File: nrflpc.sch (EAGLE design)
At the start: 62 parts, among them IC1 LPC1111/12/13/14-HVQFN33, IC3 LM3401, IC5 LM3401, IC6 LM3401, IC7 LM3401, IC8 78L05SMD, Q1 20MHz, Q2 MOSFET-PCHANNEL, Q3 MOSFET-PCHANNEL, Q4 MOSFET-PCHANNEL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

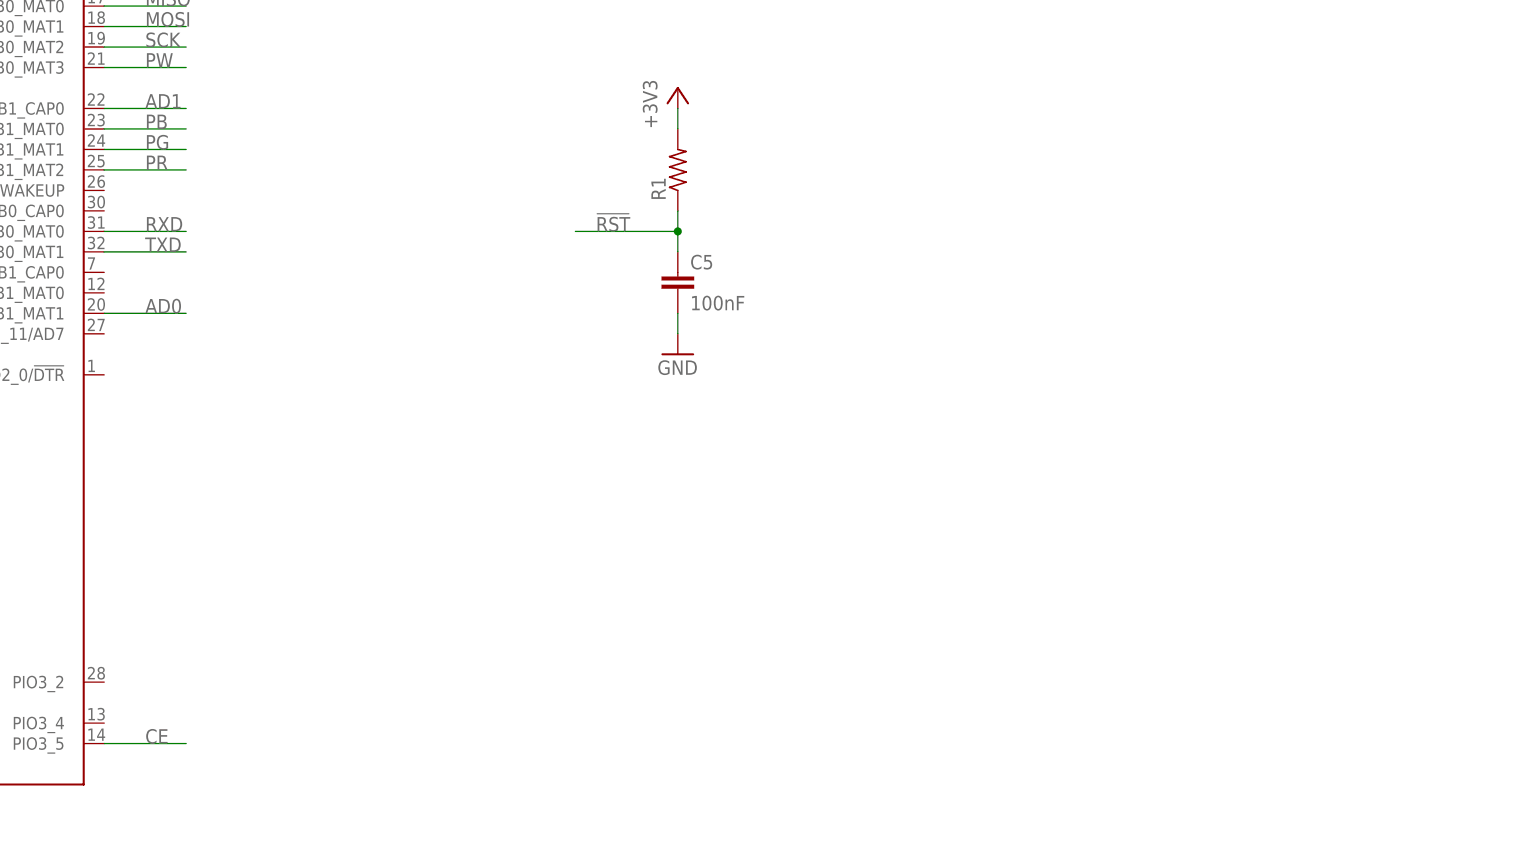
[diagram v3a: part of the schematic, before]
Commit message: ADC input filters
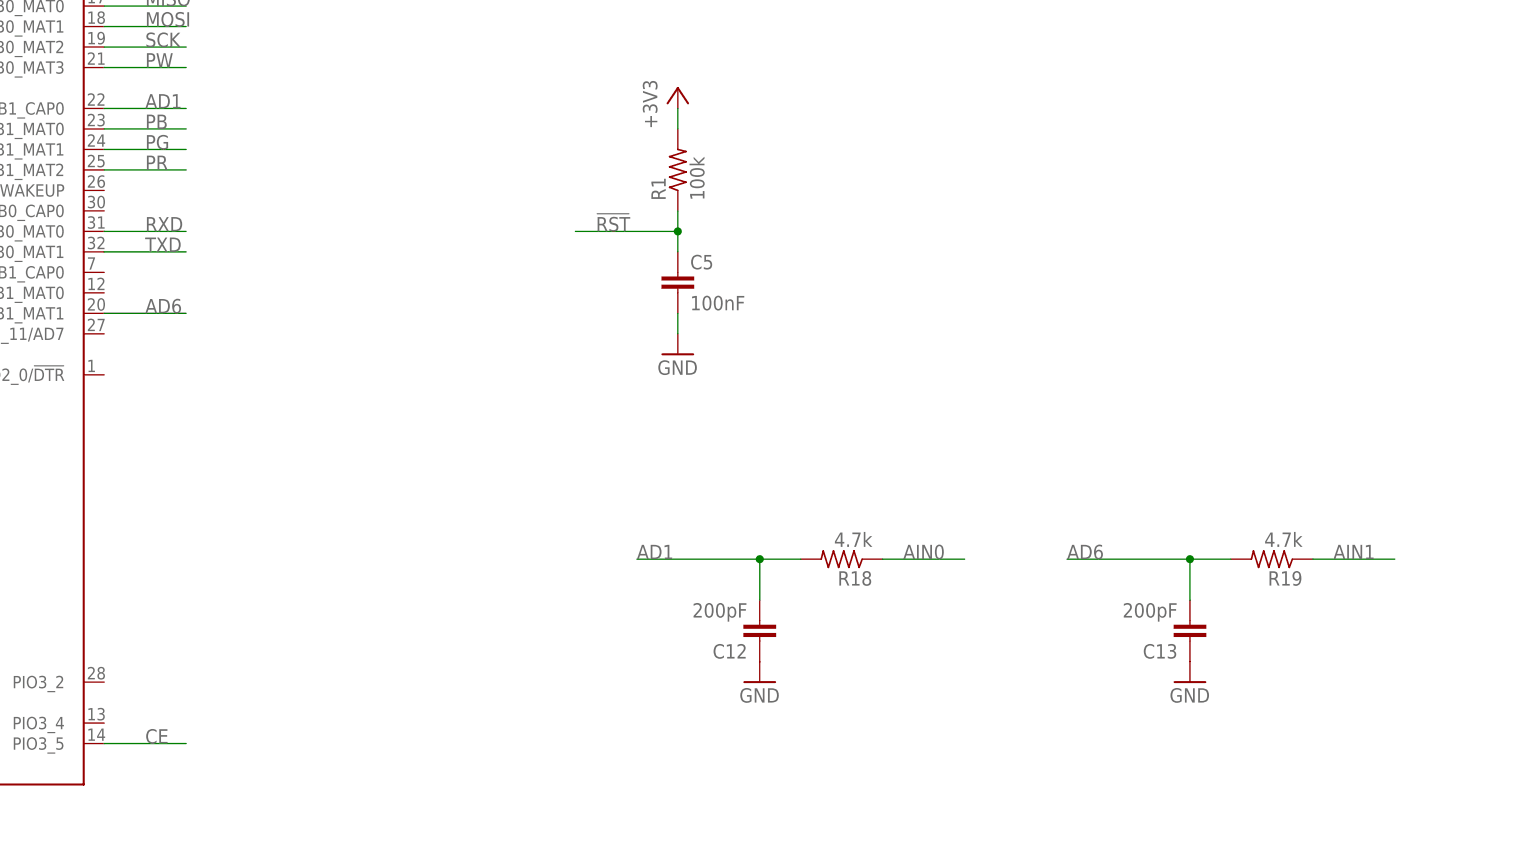
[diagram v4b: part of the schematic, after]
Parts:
- added C12, C13: 200pF, SparkFun:CAP0402-CAP
- added R18, R19: 4.7k, rcl:R-US_R0402
- R1: value (none) -> 100k
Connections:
- removed net AD0: IC1.PIO1_10/AD6/CT16B1_MAT1
- new net AD6: C13.2, IC1.PIO1_10/AD6/CT16B1_MAT1, R19.2
- new net AIN0: R18.1
- new net AIN1: R19.1
- net AD1: now also C12.2, R18.2
- net GND: now also C12.1, C13.1
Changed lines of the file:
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@@
 <part name="C4" library="rcl" deviceset="C-EU" device="C0402" value="100nF"/>
 <part name="GND5" library="supply1" deviceset="GND" device=""/>
-<part name="R1" library="rcl" deviceset="R-US_" device="R0402"/>
+<part name="R1" library="rcl" deviceset="R-US_" device="R0402" value="100k"/>
 <part name="+3V5" library="supply1" deviceset="+3V3" device=""/>
 <part name="GND13" library="supply1" deviceset="GND" device=""/>
@@
 <part name="P+1" library="supply1" deviceset="+12V" device=""/>
 <part name="GND12" library="supply1" deviceset="GND" device=""/>
+<part name="C12" library="SparkFun" deviceset="CAP" device="0402-CAP" value="200pF"/>
+<part name="R18" library="rcl" deviceset="R-US_" device="R0402" value="4.7k"/>
+<part name="GND14" library="supply1" deviceset="GND" device=""/>
+<part name="C13" library="SparkFun" deviceset="CAP" device="0402-CAP" value="200pF"/>
+<part name="R19" library="rcl" deviceset="R-US_" device="R0402" value="4.7k"/>
+<part name="GND15" library="supply1" deviceset="GND" device=""/>
 </parts>
 <sheets>
@@
 <instance part="P+1" gate="1" x="76.2" y="167.64"/>
 <instance part="GND12" gate="1" x="76.2" y="154.94"/>
+<instance part="C12" gate="G$1" x="312.42" y="101.6" rot="R180"/>
+<instance part="R18" gate="G$1" x="322.58" y="109.22" rot="R180"/>
+<instance part="GND14" gate="1" x="312.42" y="93.98"/>
+<instance part="C13" gate="G$1" x="365.76" y="101.6" rot="R180"/>
+<instance part="R19" gate="G$1" x="375.92" y="109.22" rot="R180"/>
+<instance part="GND15" gate="1" x="365.76" y="93.98"/>
 </instances>
 <busses>
@@
 <pinref part="GND12" gate="1" pin="GND"/>
 </segment>
+<segment>
+<pinref part="C12" gate="G$1" pin="1"/>
+<pinref part="GND14" gate="1" pin="GND"/>
+</segment>
+<segment>
+<pinref part="C13" gate="G$1" pin="1"/>
+<pinref part="GND15" gate="1" pin="GND"/>
+</segment>
 </net>
 <net name="!RST" class="0">
@@
 </segment>
 </net>
-<net name="AD0" class="0">
+<net name="AD6" class="0">
 <segment>
 <pinref part="IC1" gate="G$1" pin="PIO1_10/AD6/CT16B1_MAT1"/>
@@
 <label x="236.22" y="139.7" size="1.778" layer="95"/>
 </segment>
+<segment>
+<pinref part="R19" gate="G$1" pin="2"/>
+<wire x1="370.84" y1="109.22" x2="365.76" y2="109.22" width="0.1524" layer="91"/>
+<pinref part="C13" gate="G$1" pin="2"/>
+<wire x1="365.76" y1="109.22" x2="350.52" y2="109.22" width="0.1524" layer="91"/>
+<wire x1="365.76" y1="104.14" x2="365.76" y2="109.22" width="0.1524" layer="91"/>
+<junction x="365.76" y="109.22"/>
+<label x="350.52" y="109.22" size="1.778" layer="95"/>
+</segment>
 </net>
 <net name="AD1" class="0">
@@
 <label x="236.22" y="165.1" size="1.778" layer="95"/>
 </segment>
+<segment>
+<pinref part="R18" gate="G$1" pin="2"/>
+<wire x1="317.5" y1="109.22" x2="312.42" y2="109.22" width="0.1524" layer="91"/>
+<pinref part="C12" gate="G$1" pin="2"/>
+<wire x1="312.42" y1="109.22" x2="297.18" y2="109.22" width="0.1524" layer="91"/>
+<wire x1="312.42" y1="104.14" x2="312.42" y2="109.22" width="0.1524" layer="91"/>
+<junction x="312.42" y="109.22"/>
+<label x="297.18" y="109.22" size="1.778" layer="95"/>
+</segment>
 </net>
 <net name="IO0" class="0">
@@
 </segment>
 </net>
+<net name="AIN0" class="0">
+<segment>
+<pinref part="R18" gate="G$1" pin="1"/>
+<wire x1="327.66" y1="109.22" x2="337.82" y2="109.22" width="0.1524" layer="91"/>
+<label x="330.2" y="109.22" size="1.778" layer="95"/>
+</segment>
+</net>
+<net name="AIN1" class="0">
+<segment>
+<pinref part="R19" gate="G$1" pin="1"/>
+<wire x1="381" y1="109.22" x2="391.16" y2="109.22" width="0.1524" layer="91"/>
+<label x="383.54" y="109.22" size="1.778" layer="95"/>
+</segment>
+</net>

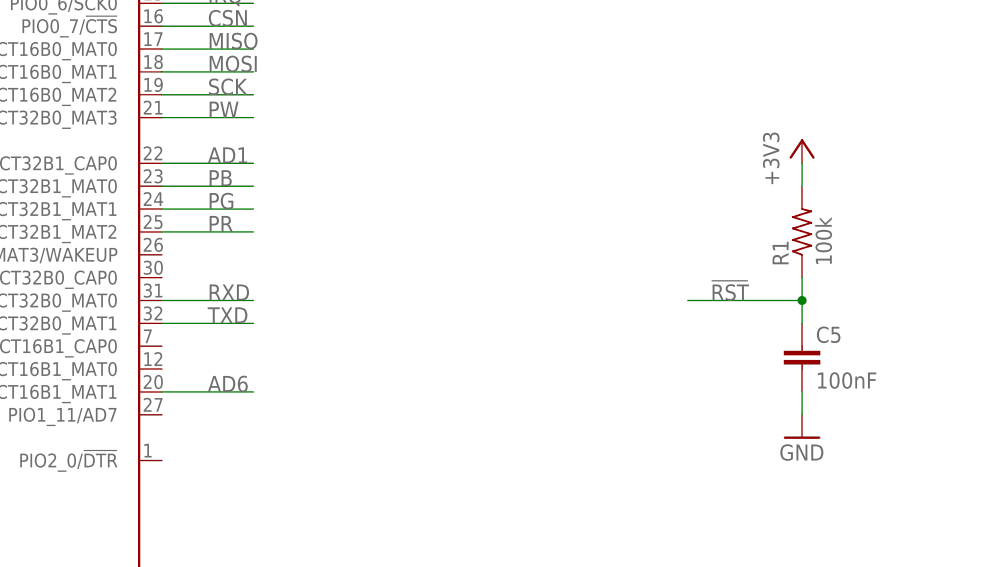
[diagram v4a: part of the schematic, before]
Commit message: UART series resistors
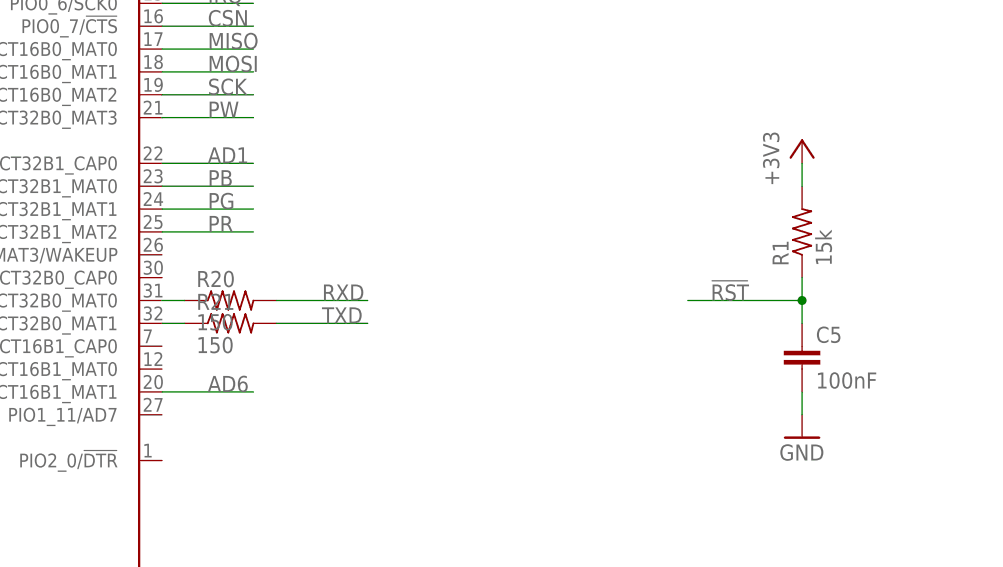
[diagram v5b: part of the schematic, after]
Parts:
- added R20, R21: 150, rcl:R-US_R0402
- R1: value 100k -> 15k
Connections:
- new net N$27: IC1.PIO1_6/RXD/CT32B0_MAT0, R20.1
- new net N$30: IC1.PIO1_7/TXD/CT32B0_MAT1, R21.1
- net RXD: now also R20.2; no longer IC1.PIO1_6/RXD/CT32B0_MAT0
- net TXD: now also R21.2; no longer IC1.PIO1_7/TXD/CT32B0_MAT1
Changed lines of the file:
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@@
 <part name="C4" library="rcl" deviceset="C-EU" device="C0402" value="100nF"/>
 <part name="GND5" library="supply1" deviceset="GND" device=""/>
-<part name="R1" library="rcl" deviceset="R-US_" device="R0402" value="100k"/>
+<part name="R1" library="rcl" deviceset="R-US_" device="R0402" value="15k"/>
 <part name="+3V5" library="supply1" deviceset="+3V3" device=""/>
 <part name="GND13" library="supply1" deviceset="GND" device=""/>
@@
 <part name="R19" library="rcl" deviceset="R-US_" device="R0402" value="4.7k"/>
 <part name="GND15" library="supply1" deviceset="GND" device=""/>
+<part name="R20" library="rcl" deviceset="R-US_" device="R0402" value="150"/>
+<part name="R21" library="rcl" deviceset="R-US_" device="R0402" value="150"/>
 </parts>
 <sheets>
@@
 <instance part="R19" gate="G$1" x="375.92" y="109.22" rot="R180"/>
 <instance part="GND15" gate="1" x="365.76" y="93.98"/>
+<instance part="R20" gate="G$1" x="238.76" y="149.86"/>
+<instance part="R21" gate="G$1" x="238.76" y="147.32"/>
 </instances>
 <busses>
@@
 </segment>
 <segment>
-<pinref part="IC1" gate="G$1" pin="PIO1_7/TXD/CT32B0_MAT1"/>
-<wire x1="231.14" y1="147.32" x2="241.3" y2="147.32" width="0.1524" layer="91"/>
-<label x="236.22" y="147.32" size="1.778" layer="95"/>
+<pinref part="R21" gate="G$1" pin="2"/>
+<wire x1="243.84" y1="147.32" x2="254" y2="147.32" width="0.1524" layer="91"/>
+<label x="248.92" y="147.32" size="1.778" layer="95"/>
 </segment>
 </net>
@@
 </segment>
 <segment>
-<pinref part="IC1" gate="G$1" pin="PIO1_6/RXD/CT32B0_MAT0"/>
-<wire x1="231.14" y1="149.86" x2="241.3" y2="149.86" width="0.1524" layer="91"/>
-<label x="236.22" y="149.86" size="1.778" layer="95"/>
+<pinref part="R20" gate="G$1" pin="2"/>
+<wire x1="243.84" y1="149.86" x2="254" y2="149.86" width="0.1524" layer="91"/>
+<label x="248.92" y="149.86" size="1.778" layer="95"/>
 </segment>
 </net>
@@
 </segment>
 </net>
+<net name="N$27" class="0">
+<segment>
+<pinref part="IC1" gate="G$1" pin="PIO1_6/RXD/CT32B0_MAT0"/>
+<pinref part="R20" gate="G$1" pin="1"/>
+<wire x1="231.14" y1="149.86" x2="233.68" y2="149.86" width="0.1524" layer="91"/>
+</segment>
+</net>
+<net name="N$30" class="0">
+<segment>
+<pinref part="IC1" gate="G$1" pin="PIO1_7/TXD/CT32B0_MAT1"/>
+<pinref part="R21" gate="G$1" pin="1"/>
+<wire x1="231.14" y1="147.32" x2="233.68" y2="147.32" width="0.1524" layer="91"/>
+</segment>
+</net>

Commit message: Routing Power supply, in progress
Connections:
- removed net N$18: C16.2, IC8G$1.VIN
- net +12V: now also C16.2, IC8G$1.VIN
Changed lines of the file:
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@@
 <pinref part="P+1" gate="1" pin="+12V"/>
+</segment>
+<segment>
+<wire x1="187.96" y1="48.26" x2="193.04" y2="48.26" width="0.1524" layer="91"/>
+<wire x1="193.04" y1="45.72" x2="193.04" y2="48.26" width="0.1524" layer="91"/>
+<pinref part="C16" gate="G$1" pin="2"/>
+<pinref part="P+6" gate="1" pin="+12V"/>
+<pinref part="IC8" gate="G$1" pin="VIN"/>
+<wire x1="198.12" y1="48.26" x2="193.04" y2="48.26" width="0.1524" layer="91"/>
+<junction x="193.04" y="48.26"/>
 </segment>
 </net>
@@
 </segment>
 </net>
-<net name="N$18" class="0">
-<segment>
-<wire x1="187.96" y1="48.26" x2="193.04" y2="48.26" width="0.1524" layer="91"/>
-<wire x1="193.04" y1="48.26" x2="198.12" y2="48.26" width="0.1524" layer="91"/>
-<wire x1="193.04" y1="45.72" x2="193.04" y2="48.26" width="0.1524" layer="91"/>
-<junction x="193.04" y="48.26"/>
-<pinref part="IC8" gate="G$1" pin="VIN"/>
-<pinref part="C16" gate="G$1" pin="2"/>
-<pinref part="P+6" gate="1" pin="+12V"/>
-</segment>
-</net>

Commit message: Layout
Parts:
- added IC2: LT1763CS8-3.3, linear-technology:LT1763CS8-3.3
- added R22: 150, rcl:R-US_R0402
- added R23: 15k, rcl:R-US_R0402
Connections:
- new net BOOTL: R22.2
- new net N$18: IC1.PIO0_1/CLKOUT/CT32B0_MAT2, R22.1, R23.1
- net +3V3: now also R23.2
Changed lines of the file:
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@@
 <part name="R20" library="rcl" deviceset="R-US_" device="R0402" value="150"/>
 <part name="R21" library="rcl" deviceset="R-US_" device="R0402" value="150"/>
+<part name="IC2" library="linear-technology" deviceset="LT1763CS8" device="" technology="-3.3"/>
+<part name="R22" library="rcl" deviceset="R-US_" device="R0402" value="150"/>
+<part name="R23" library="rcl" deviceset="R-US_" device="R0402" value="15k"/>
+<part name="+3V3" library="supply1" deviceset="+3V3" device=""/>
 </parts>
 <sheets>
@@
 <instance part="R20" gate="G$1" x="238.76" y="149.86"/>
 <instance part="R21" gate="G$1" x="238.76" y="147.32"/>
+<instance part="IC2" gate="G$1" x="254" y="60.96"/>
+<instance part="R22" gate="G$1" x="256.54" y="195.58"/>
+<instance part="R23" gate="G$1" x="248.92" y="203.2" rot="R90"/>
+<instance part="+3V3" gate="G$1" x="248.92" y="213.36"/>
 </instances>
 <busses>
@@
 <wire x1="302.26" y1="165.1" x2="302.26" y2="162.56" width="0.1524" layer="91"/>
 </segment>
+<segment>
+<pinref part="+3V3" gate="G$1" pin="+3V3"/>
+<pinref part="R23" gate="G$1" pin="2"/>
+<wire x1="248.92" y1="210.82" x2="248.92" y2="208.28" width="0.1524" layer="91"/>
+</segment>
 </net>
 <net name="CE" class="0">
@@
 </segment>
 </net>
+<net name="N$18" class="0">
+<segment>
+<pinref part="IC1" gate="G$1" pin="PIO0_1/CLKOUT/CT32B0_MAT2"/>
+<wire x1="231.14" y1="195.58" x2="248.92" y2="195.58" width="0.1524" layer="91"/>
+<pinref part="R22" gate="G$1" pin="1"/>
+<pinref part="R23" gate="G$1" pin="1"/>
+<wire x1="248.92" y1="195.58" x2="251.46" y2="195.58" width="0.1524" layer="91"/>
+<wire x1="248.92" y1="198.12" x2="248.92" y2="195.58" width="0.1524" layer="91"/>
+<junction x="248.92" y="195.58"/>
+</segment>
+</net>
+<net name="BOOTL" class="0">
+<segment>
+<pinref part="R22" gate="G$1" pin="2"/>
+<wire x1="261.62" y1="195.58" x2="269.24" y2="195.58" width="0.1524" layer="91"/>
+<label x="261.62" y="195.58" size="1.778" layer="95"/>
+</segment>
+</net>
